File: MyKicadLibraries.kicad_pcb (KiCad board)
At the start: 2 copper layers, 184.4 x 134.7 mm, 45 parts, among them J1 Conn_01x08, J10 RCJ-22, J11 DIN-5, J12 Mini-DIN-6, J13 USB_A, J14 Conn_01x02, J15 Conn_01x02, J2 Conn_01x08, J3 POGO Pins, J4 c8-inlet, J5 FTDI, J6 Micro_SD_Card, J7 Conn_01x04, J8 Conn_02x04_Counter_Clockwise, J9 Conn_01x04, SW1 Schurter Switch, SW2 POWER, U1 radio-receiver, U10 rdm-6300, U11 magnetic-charger, U12 adafruit-MAX98357, U13 TTL, U14 lxb18, U15 esp32-wemos-d1-mini, U16 TCRT5000, U17 opb607a, U18 max98367, U19 esp-01f, U2 tp4056, U20 m18, U21 bme280, U23 mems-mic, U26 C3 Pico, U3 LilygoSIMT7000G, U4 esp-01m, U5 relais_module, U6 ESP-01, U7 dcdc, U8 mems-mic, U9 ESP-12E

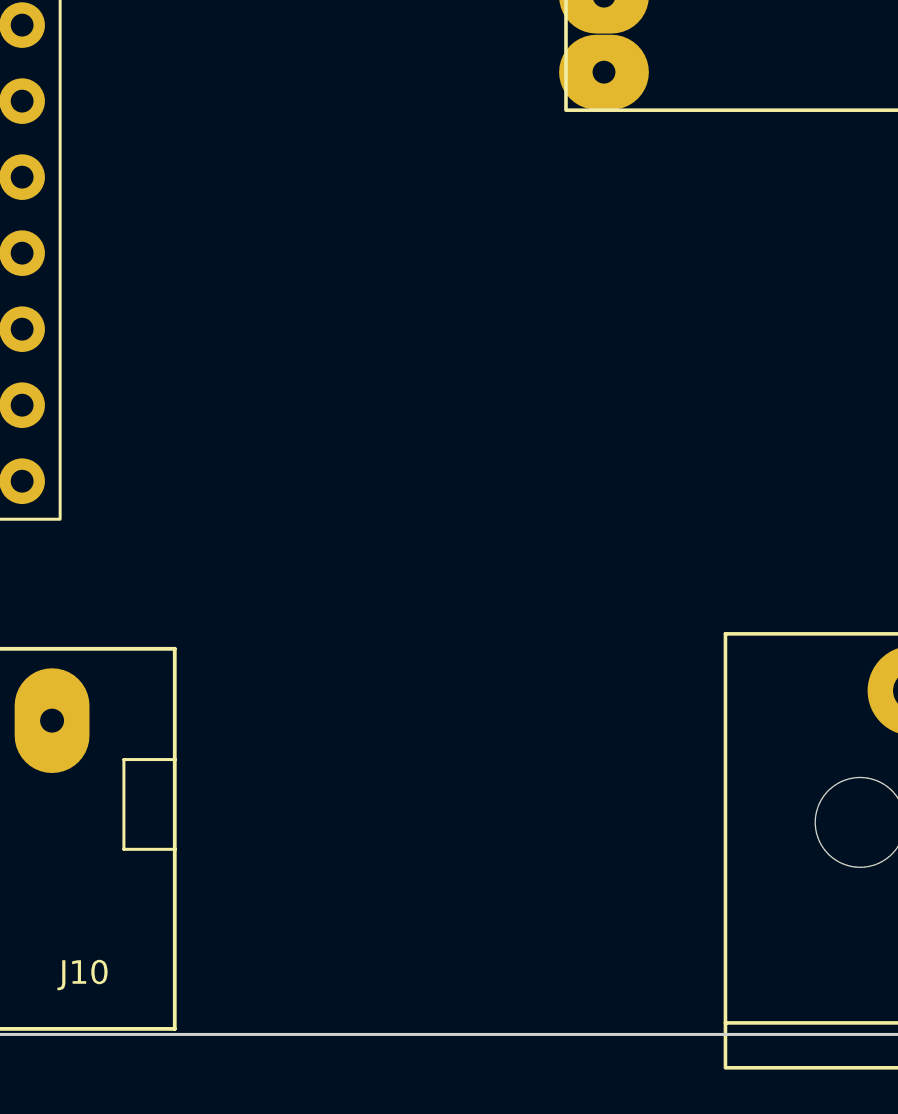
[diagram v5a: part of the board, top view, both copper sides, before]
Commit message: Add QWIIC adapter
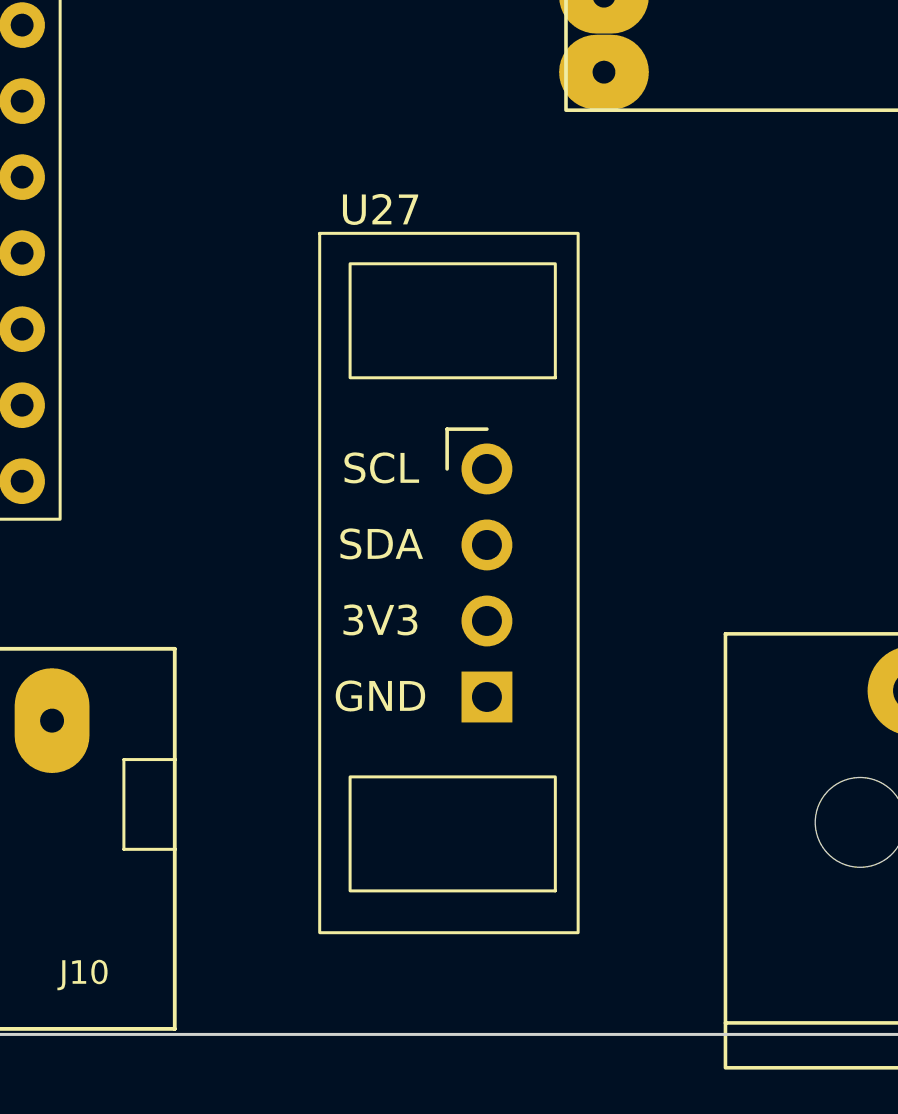
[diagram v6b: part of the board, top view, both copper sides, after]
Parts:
- added U27: ~, qwiic-adapter:qwiic-adapter, F.Cu at (176.5, 152.4)
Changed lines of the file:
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@@
   (net 329 "unconnected-(U26-IO3{slash}VBAT-Pad15)")
   (net 330 "unconnected-(U26-RST{slash}EN-Pad16)")
+  (net 331 "unconnected-(U27-GND-Pad1)")
+  (net 332 "unconnected-(U27-3V3-Pad2)")
+  (net 333 "unconnected-(U27-SDA-Pad3)")
+  (net 334 "unconnected-(U27-SCL-Pad4)")
   (footprint "esp-01f:esp-01f" (layer "F.Cu")
     (at 114.405 137.985)
@@
     )
   )
+  (footprint "qwiic-adapter:qwiic-adapter" (layer "F.Cu")
+    (at 176.53 152.402)
+    (descr "Through hole straight pin header, 1x04, 2.54mm pitch, single row")
+    (tags "Through hole pin header THT 1x04 2.54mm single row")
+    (property "Sheetfile" "MyKicadLibraries.kicad_sch")
+    (property "Sheetname" "")
+    (attr through_hole)
+    (fp_text reference "U27" (at -3.556 -12.446) (layer "F.SilkS")
+        (effects (font (size 1 1) (thickness 0.15)))
+    )
+    (fp_text value "~" (at 0 9.95) (layer "F.Fab")
+        (effects (font (size 1 1) (thickness 0.15)))
+    )
+    (fp_text user "SCL" (at -3.556 -3.81) (layer "F.SilkS")
+        (effects (font (size 1 1) (thickness 0.1)))
+    )
+    (fp_text user "SDA" (at -3.556 -1.27) (layer "F.SilkS")
+        (effects (font (size 1 1) (thickness 0.1)))
+    )
+    (fp_text user "GND" (at -3.556 3.81) (layer "F.SilkS")
+        (effects (font (size 1 1) (thickness 0.1)))
+    )
+    (fp_text user "3V3" (at -3.556 1.27) (layer "F.SilkS")
+        (effects (font (size 1 1) (thickness 0.1)))
+    )
+    (fp_text user "${REFERENCE}" (at 0 -0.002 90) (layer "F.Fab")
+        (effects (font (size 1 1) (thickness 0.15)))
+    )
+    (fp_line (start -1.33 -5.142) (end 0 -5.142)
+      (stroke (width 0.12) (type solid)) (layer "F.SilkS"))
+    (fp_line (start -1.33 -3.812) (end -1.33 -5.142)
+      (stroke (width 0.12) (type solid)) (layer "F.SilkS"))
+    (fp_rect (start -5.588 -11.684) (end 3.048 11.684)
+      (stroke (width 0.1) (type default)) (fill none) (layer "F.SilkS"))
+    (fp_rect (start 2.286 -6.858) (end -4.572 -10.668)
+      (stroke (width 0.1) (type default)) (fill none) (layer "F.SilkS"))
+    (fp_rect (start 2.286 10.287) (end -4.572 6.477)
+      (stroke (width 0.1) (type default)) (fill none) (layer "F.SilkS"))
+    (fp_line (start -5.588 -11.684) (end -5.588 11.684)
+      (stroke (width 0.05) (type solid)) (layer "F.CrtYd"))
+    (fp_line (start -5.588 11.684) (end 3.048 11.684)
+      (stroke (width 0.05) (type solid)) (layer "F.CrtYd"))
+    (fp_line (start 3.048 -11.684) (end -5.588 -11.684)
+      (stroke (width 0.05) (type solid)) (layer "F.CrtYd"))
+    (fp_line (start 3.048 11.684) (end 3.048 -11.684)
+      (stroke (width 0.05) (type solid)) (layer "F.CrtYd"))
+    (fp_line (start -1.27 -4.447) (end -0.635 -5.082)
+      (stroke (width 0.1) (type solid)) (layer "F.Fab"))
+    (fp_line (start -1.27 5.078) (end -1.27 -4.447)
+      (stroke (width 0.1) (type solid)) (layer "F.Fab"))
+    (fp_line (start -0.635 -5.082) (end 1.27 -5.082)
+      (stroke (width 0.1) (type solid)) (layer "F.Fab"))
+    (fp_line (start 1.27 -5.082) (end 1.27 5.078)
+      (stroke (width 0.1) (type solid)) (layer "F.Fab"))
+    (fp_line (start 1.27 5.078) (end -1.27 5.078)
+      (stroke (width 0.1) (type solid)) (layer "F.Fab"))
+    (pad "1" thru_hole rect (at 0 3.808) (size 1.7 1.7) (drill 1) (layers "*.Cu" "*.Mask")
+      (net 331 "unconnected-(U27-GND-Pad1)") (pinfunction "GND") (pintype "power_in"))
+    (pad "2" thru_hole oval (at 0 1.268) (size 1.7 1.7) (drill 1) (layers "*.Cu" "*.Mask")
+      (net 332 "unconnected-(U27-3V3-Pad2)") (pinfunction "3V3") (pintype "power_in"))
+    (pad "3" thru_hole oval (at 0 -1.272) (size 1.7 1.7) (drill 1) (layers "*.Cu" "*.Mask")
+      (net 333 "unconnected-(U27-SDA-Pad3)") (pinfunction "SDA") (pintype "bidirectional"))
+    (pad "4" thru_hole circle (at 0 -3.812) (size 1.7 1.7) (drill 1) (layers "*.Cu" "*.Mask")
+      (net 334 "unconnected-(U27-SCL-Pad4)") (pinfunction "SCL") (pintype "input"))
+    (model "${KICAD6_3DMODEL_DIR}/Connector_PinHeader_2.54mm.3dshapes/PinHeader_1x04_P2.54mm_Vertical.wrl"
+      (offset (xyz 0 3.81 0))
+      (scale (xyz 1 1 1))
+      (rotate (xyz 0 0 0))
+    )
+    (model "${KIPRJMOD}/lib/qwiic-adapter/qwiic-adapter.step"
+      (offset (xyz -1.27 0 2.54))
+      (scale (xyz 1 1 1))
+      (rotate (xyz 0 0 90))
+    )
+  )

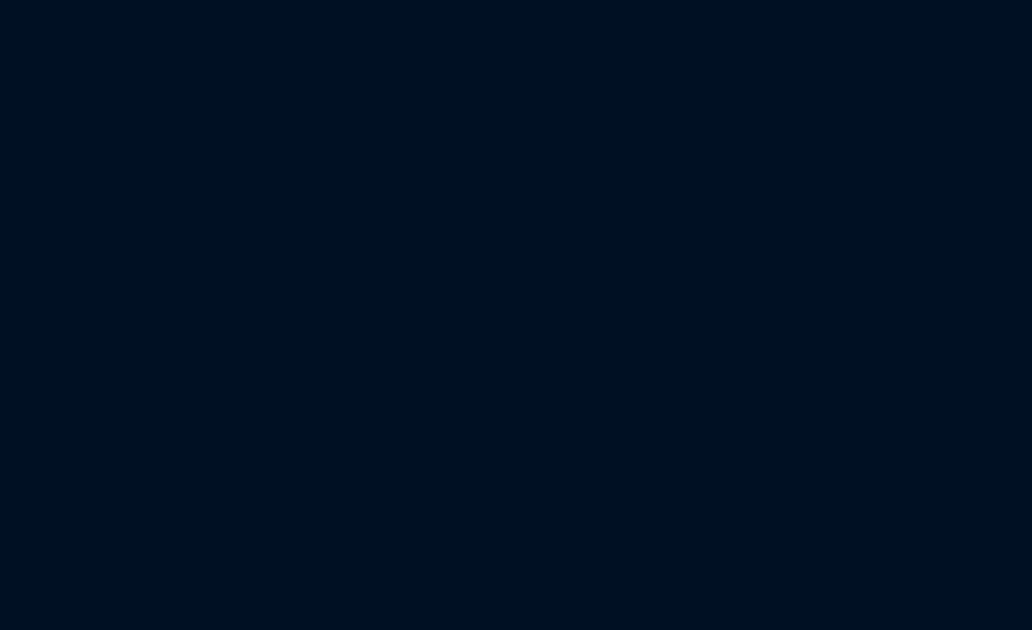
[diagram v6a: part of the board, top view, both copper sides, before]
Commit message: Add DCF77
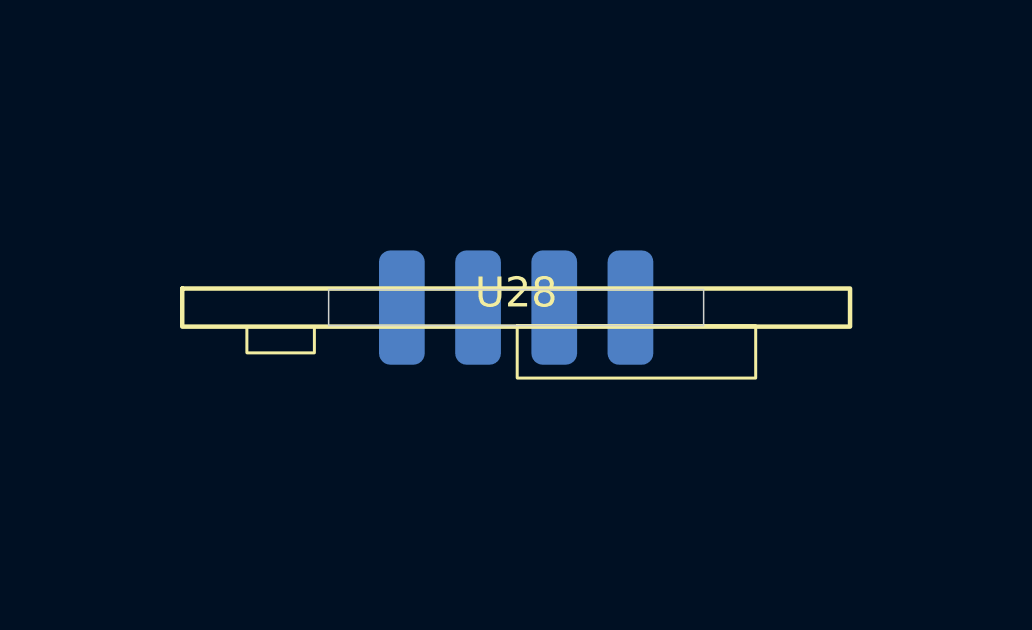
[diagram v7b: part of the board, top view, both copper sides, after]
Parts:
- added U28: DCF-77, dcf77:dcf77, F.Cu at (225.4, 59.1)
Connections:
- U27 pad 1: unconnected-(U27-GND-Pad1) -> GND
